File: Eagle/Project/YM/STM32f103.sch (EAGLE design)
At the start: 76 parts, among them IC1 YM3812, IC10 YM3812, IC11 YM3014B, IC12 LM358N, IC13 BA033CC0T, IC14 74ALS04N, IC15 6N136, IC2 YM3014B, IC3 LM358N, IC4 YM3812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

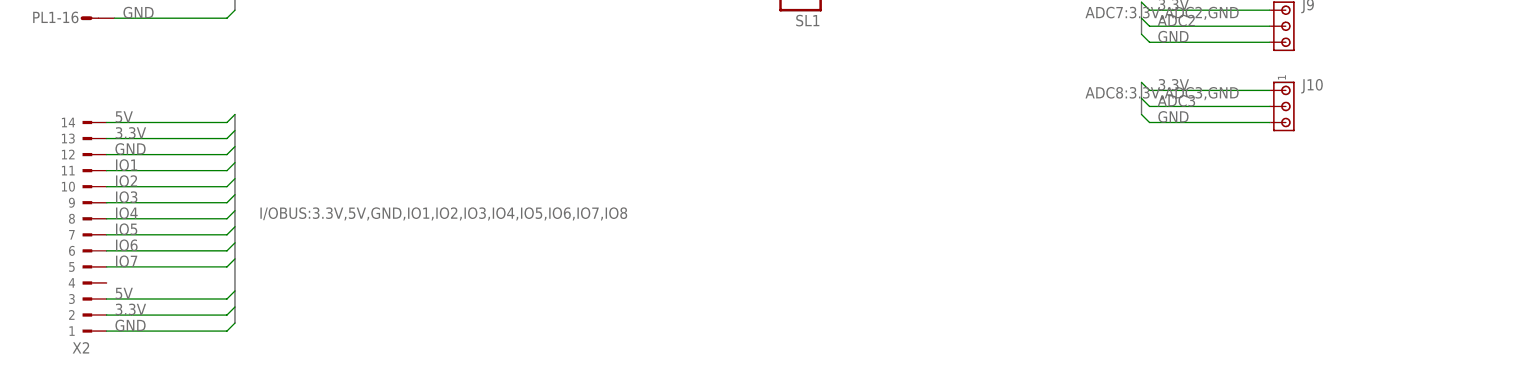
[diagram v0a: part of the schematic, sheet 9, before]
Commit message: LCD BOOTLOADER HEADER
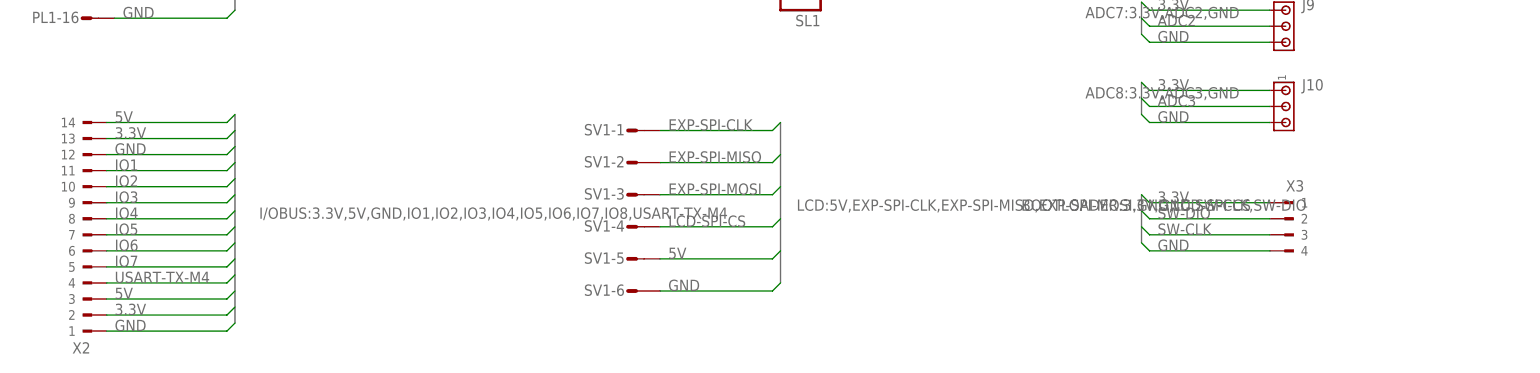
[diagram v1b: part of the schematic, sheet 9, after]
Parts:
- added SV1: (no value), con-amp-mt:S06P
- added X3: (no value), con-weidmueller-sl35:90F-4
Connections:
- new net LCD-SPI-CS: SV1-4.S, U1PORTA_L.PA2
- net 3.3V: now also X3.1
- net 5V: now also SV1-5.S
- net EXP-SPI-CLK: now also SV1-1.S
- net EXP-SPI-MISO: now also SV1-2.S
- net EXP-SPI-MOSI: now also SV1-3.S
- net GND: now also SV1-6.S, X3.4
- net IO7: no longer U1PORTA_L.PA2
- net SW-CLK: now also X3.3
- net SW-DIO: now also X3.2
- net USART-TX-M4: now also X2.4
- net YM1-CS: no longer U1PORTC_H.PC10
- net YM2-CS: now also U1PORTC_H.PC10

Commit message: Eerste versie PCB - Nog niet gerout/gerouted/geroutedt. Ter review voor plaatsing componenten.
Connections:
- removed net N$28: C39.2
- net 5V: now also C39.2
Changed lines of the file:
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@@
 <pinref part="IC14" gate="P" pin="VCC"/>
 <wire x1="175.26" y1="101.6" x2="208.28" y2="101.6" width="0.1524" layer="91"/>
+<pinref part="C39" gate="G$1" pin="2"/>
+<wire x1="208.28" y1="93.98" x2="208.28" y2="101.6" width="0.1524" layer="91"/>
+<wire x1="208.28" y1="101.6" x2="208.28" y2="109.22" width="0.1524" layer="91"/>
+<junction x="208.28" y="101.6"/>
 </segment>
 </net>
@@
 </segment>
 </net>
-<net name="N$28" class="0">
-<segment>
-<pinref part="C39" gate="G$1" pin="2"/>
-<wire x1="208.28" y1="93.98" x2="208.28" y2="109.22" width="0.1524" layer="91"/>
-</segment>
-</net>

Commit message: Opamp wire change
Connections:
- removed net N$13: C29.1, IC11.MP, IC12B.-IN
- new net N$15: C13.1, IC2.RB, IC3B.+IN
- net N$10: now also C28.1, IC11.RB, IC12B.+IN; no longer C24.1, IC8.MP, IC9B.-IN
- net N$11: now also C24.1, IC8.MP, IC9B.-IN; no longer C23.1, IC8.RB, IC9B.+IN
- net N$14: now also C29.1, IC11.MP, IC12B.-IN; no longer C28.1, IC11.RB, IC12B.+IN
- net N$4: now also C18.1, IC5.RB, IC6B.+IN; no longer C14.1, IC2.MP, IC3B.-IN
- net N$5: now also C14.1, IC2.MP, IC3B.-IN; no longer C13.1, IC2.RB, IC3B.+IN
- net N$7: now also C23.1, IC8.RB, IC9B.+IN; no longer C19.1, IC5.MP, IC6B.-IN
- net N$8: now also C19.1, IC5.MP, IC6B.-IN; no longer C18.1, IC5.RB, IC6B.+IN

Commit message: v2.0 - voldoet aan de DRC van JLPCB - PCB staat klaar voor review project groep.
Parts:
- removed X3: (no value), con-weidmueller-sl35:90F-4
- added SV2: (no value), con-lstb:MA04-1
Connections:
- net 3.3V: now also SV2.1; no longer X3.1
- net GND: now also SV2.4; no longer X3.4
- net SW-CLK: now also SV2.3; no longer X3.3
- net SW-DIO: now also SV2.2; no longer X3.2
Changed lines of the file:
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@@
 <part name="SL1" library="con-amp-quick" library_urn="urn:adsk.eagle:library:125" deviceset="M16" device="" package3d_urn="urn:adsk.eagle:package:5969/1"/>
 <part name="SV1" library="con-amp-mt" library_urn="urn:adsk.eagle:library:123" deviceset="S06P" device="" package3d_urn="urn:adsk.eagle:package:5792/1"/>
-<part name="X3" library="con-weidmueller-sl35" library_urn="urn:adsk.eagle:library:199" deviceset="90F-4" device="" package3d_urn="urn:adsk.eagle:package:11425/1"/>
+<part name="SV2" library="con-lstb" library_urn="urn:adsk.eagle:library:162" deviceset="MA04-1" device="" package3d_urn="urn:adsk.eagle:package:8337/1"/>
 </parts>
 <sheets>
@@
 <attribute name="VALUE" x="115.824" y="31.877" size="1.778" layer="96"/>
 </instance>
-<instance part="X3" gate="G$1" x="219.71" y="45.72" smashed="yes">
-<attribute name="NAME" x="219.71" y="50.038" size="1.778" layer="95"/>
-<attribute name="VALUE" x="219.71" y="37.084" size="1.778" layer="96"/>
+<instance part="SV2" gate="1" x="226.06" y="43.18" smashed="yes" rot="R180">
+<attribute name="VALUE" x="227.33" y="53.34" size="1.778" layer="96" rot="R180"/>
+<attribute name="NAME" x="227.33" y="37.338" size="1.778" layer="95" rot="R180"/>
 </instance>
 </instances>
@@
 </segment>
 <segment>
-<pinref part="X3" gate="G$1" pin="1"/>
-<wire x1="217.17" y1="48.26" x2="198.12" y2="48.26" width="0.1524" layer="91"/>
+<wire x1="218.44" y1="48.26" x2="198.12" y2="48.26" width="0.1524" layer="91"/>
 <wire x1="198.12" y1="48.26" x2="196.85" y2="49.53" width="0.1524" layer="91"/>
 <label x="199.39" y="48.26" size="1.778" layer="95"/>
+<pinref part="SV2" gate="1" pin="1"/>
 </segment>
 </net>
@@
 </segment>
 <segment>
-<pinref part="X3" gate="G$1" pin="4"/>
-<wire x1="217.17" y1="40.64" x2="198.12" y2="40.64" width="0.1524" layer="91"/>
+<wire x1="218.44" y1="40.64" x2="198.12" y2="40.64" width="0.1524" layer="91"/>
 <wire x1="198.12" y1="40.64" x2="196.85" y2="41.91" width="0.1524" layer="91"/>
 <label x="199.39" y="40.64" size="1.778" layer="95"/>
+<pinref part="SV2" gate="1" pin="4"/>
 </segment>
 </net>
@@
 <net name="SW-DIO" class="0">
 <segment>
-<pinref part="X3" gate="G$1" pin="2"/>
-<wire x1="217.17" y1="45.72" x2="198.12" y2="45.72" width="0.1524" layer="91"/>
+<wire x1="218.44" y1="45.72" x2="198.12" y2="45.72" width="0.1524" layer="91"/>
 <wire x1="198.12" y1="45.72" x2="196.85" y2="46.99" width="0.1524" layer="91"/>
 <label x="199.39" y="45.72" size="1.778" layer="95"/>
+<pinref part="SV2" gate="1" pin="2"/>
 </segment>
 </net>
 <net name="SW-CLK" class="0">
 <segment>
-<pinref part="X3" gate="G$1" pin="3"/>
-<wire x1="217.17" y1="43.18" x2="198.12" y2="43.18" width="0.1524" layer="91"/>
+<wire x1="218.44" y1="43.18" x2="198.12" y2="43.18" width="0.1524" layer="91"/>
 <wire x1="198.12" y1="43.18" x2="196.85" y2="44.45" width="0.1524" layer="91"/>
 <label x="199.39" y="43.18" size="1.778" layer="95"/>
+<pinref part="SV2" gate="1" pin="3"/>
 </segment>
 </net>

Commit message: v2.5 - IO expander update - moet nog steeds gepeerreviewd worden.
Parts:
- removed PL1: (no value), con-harting-v:16VS
- added SV3: 2514-6002UB, 2514-6002UB:2514-6002UB
- C10, C9: value (none) -> 20pF
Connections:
- removed net EXP-SPI-A0: PL1-7.S, U1PORTC_L.PC6
- removed net EXP-SPI-A1: PL1-8.S, U1PORTC_L.PC7
- removed net EXP-SPI-NSS: PL1-12.S, U1PORTB_H.PB12
- removed net EXP3-INTA: PL1-5.S, U1PORTA_H.PA11
- removed net EXP3-INTB: PL1-6.S, U1PORTA_H.PA12
- new net EXP-SPI-NSS0: SV3.11, U1PORTC_L.PC6
- new net EXP-SPI-NSS1: SV3.10, U1PORTC_L.PC7
- new net OPEN: SV3.1
- net 3.3V: now also SV3.4; no longer PL1-14.S
- net 5V: now also SV3.3; no longer PL1-15.S
- net EXP-RST: now also SV3.9; no longer PL1-13.S
- net EXP-SPI-CLK: now also SV3.14; no longer PL1-9.S
- net EXP-SPI-MISO: now also SV3.13; no longer PL1-10.S
- net EXP-SPI-MOSI: now also SV3.12; no longer PL1-11.S
- net EXP1-INTA: now also SV3.8; no longer PL1-1.S
- net EXP1-INTB: now also SV3.7; no longer PL1-2.S
- net EXP2-INTA: now also SV3.5; no longer PL1-3.S
- net EXP2-INTB: now also SV3.6; no longer PL1-4.S
- net GND: now also SV3.2; no longer PL1-16.S
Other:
- moved on the sheet: C12, C17, C22, C27, U1PORTA_H, U1PORTC_H, U1PORTC_L

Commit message: v3.0 - PCB review aangepast
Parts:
- removed X2: (no value), con-weidmueller-sl35:180G-14
- added SV4: (no value), con-lsta:FE13-1
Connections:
- removed net IO7: X2.5
- net 3.3V: now also SV4.12, SV4.2; no longer X2.13, X2.2
- net 5V: now also SV4.13, SV4.3; no longer X2.14, X2.3
- net GND: now also SV4.1, SV4.11; no longer X2.1, X2.12
- net IO1: now also SV4.10; no longer X2.11
- net IO2: now also SV4.9; no longer X2.10
- net IO3: now also SV4.8; no longer X2.9
- net IO4: now also SV4.7; no longer X2.8
- net IO5: now also SV4.6; no longer X2.7
- net IO6: now also SV4.5; no longer X2.6
- net USART-TX-M4: now also SV4.4; no longer X2.4
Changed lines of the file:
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@@
 <part name="J9" library="con-amp" library_urn="urn:adsk.eagle:library:127" deviceset="MTA03-156" device="" package3d_urn="urn:adsk.eagle:package:8081563/1"/>
 <part name="J10" library="con-amp" library_urn="urn:adsk.eagle:library:127" deviceset="MTA03-156" device="" package3d_urn="urn:adsk.eagle:package:8081563/1"/>
-<part name="X2" library="con-weidmueller-sl35" library_urn="urn:adsk.eagle:library:199" deviceset="180G-14" device="" package3d_urn="urn:adsk.eagle:package:11378/1"/>
 <part name="J2" library="SparkFun-Connectors" library_urn="urn:adsk.eagle:library:513" deviceset="DIN5" device="" package3d_urn="urn:adsk.eagle:package:38294/1"/>
 <part name="D1" library="BAT20JFILM" deviceset="BAT20JFILM" device=""/>
@@
 <part name="SV2" library="con-lstb" library_urn="urn:adsk.eagle:library:162" deviceset="MA04-1" device="" package3d_urn="urn:adsk.eagle:package:8337/1"/>
 <part name="SV3" library="2514-6002UB" deviceset="2514-6002UB" device=""/>
+<part name="SV4" library="con-lsta" library_urn="urn:adsk.eagle:library:161" deviceset="FE13-1" device="" package3d_urn="urn:adsk.eagle:package:8213/1"/>
 </parts>
 <sheets>
@@
 <attribute name="VALUE" x="215.9" y="58.42" size="1.778" layer="96" rot="R270"/>
 </instance>
-<instance part="X2" gate="G$1" x="30.48" y="43.18" smashed="yes" rot="R180">
-<attribute name="NAME" x="30.48" y="26.162" size="1.778" layer="95" rot="R180"/>
-<attribute name="VALUE" x="30.48" y="64.516" size="1.778" layer="96" rot="R180"/>
-</instance>
 <instance part="SL2" gate="G$1" x="140.97" y="142.24" smashed="yes" rot="R180">
 <attribute name="VALUE" x="146.05" y="152.4" size="1.778" layer="96" rot="R180"/>
@@
 <attribute name="VALUE" x="45.6184" y="119.761" size="2.0828" layer="96" ratio="10" rot="SR0"/>
 </instance>
+<instance part="SV4" gate="G$1" x="29.21" y="86.36" smashed="yes">
+<attribute name="VALUE" x="27.94" y="66.04" size="1.778" layer="96"/>
+<attribute name="NAME" x="27.94" y="104.902" size="1.778" layer="95"/>
+</instance>
 </instances>
 <busses>
@@
 </segment>
 </bus>
-<bus name="I/OBUS:3.3V,5V,GND,IO1,IO2,IO3,IO4,IO5,IO6,IO7,IO8,USART-TX-M4">
-<segment>
-<wire x1="53.34" y1="62.23" x2="53.34" y2="29.21" width="0.762" layer="92"/>
-<label x="57.15" y="45.72" size="1.778" layer="95"/>
-</segment>
-</bus>
 <bus name="YM-DIG-OUTPUT:5V,GND,USART-RX-M4,USART-TX-M4,YM1-CLK-O,YM1-CS,YM1-OUTPUT,YM1-SYNC,YM2-CLK-O,YM2-OUTPUT,YM2-SYNC,YM3-CLK-O,YM3-OUTPUT,YM3-SYNC,YM4-CLK-O,YM4-OUTPUT,YM4-SYNC">
 <segment>
@@
 <net name="5V" class="0">
 <segment>
-<wire x1="33.02" y1="60.96" x2="52.07" y2="60.96" width="0.1524" layer="91"/>
-<wire x1="52.07" y1="60.96" x2="53.34" y2="62.23" width="0.1524" layer="91"/>
-<label x="34.29" y="60.96" size="1.778" layer="95"/>
-<pinref part="X2" gate="G$1" pin="14"/>
-</segment>
-<segment>
-<pinref part="X2" gate="G$1" pin="3"/>
-<wire x1="33.02" y1="33.02" x2="52.07" y2="33.02" width="0.1524" layer="91"/>
-<wire x1="52.07" y1="33.02" x2="53.34" y2="34.29" width="0.1524" layer="91"/>
-<label x="34.29" y="33.02" size="1.778" layer="95"/>
-</segment>
-<segment>
 <pinref part="SL1" gate="G$1" pin="15"/>
 <wire x1="135.89" y1="83.82" x2="116.84" y2="83.82" width="0.1524" layer="91"/>
@@
 <wire x1="31.75" y1="142.24" x2="13.97" y2="142.24" width="0.1524" layer="91"/>
 </segment>
+<segment>
+<pinref part="SV4" gate="G$1" pin="13"/>
+<wire x1="36.83" y1="101.6" x2="54.61" y2="101.6" width="0.1524" layer="91"/>
+<label x="38.1" y="101.6" size="1.778" layer="95"/>
+</segment>
+<segment>
+<pinref part="SV4" gate="G$1" pin="3"/>
+<wire x1="36.83" y1="76.2" x2="54.61" y2="76.2" width="0.1524" layer="91"/>
+<label x="38.1" y="76.2" size="1.778" layer="95"/>
+</segment>
 </net>
 <net name="3.3V" class="0">
@@
 </segment>
 <segment>
-<wire x1="33.02" y1="58.42" x2="52.07" y2="58.42" width="0.1524" layer="91"/>
-<wire x1="52.07" y1="58.42" x2="53.34" y2="59.69" width="0.1524" layer="91"/>
-<label x="34.29" y="58.42" size="1.778" layer="95"/>
-<pinref part="X2" gate="G$1" pin="13"/>
-</segment>
-<segment>
-<pinref part="X2" gate="G$1" pin="2"/>
-<wire x1="33.02" y1="30.48" x2="52.07" y2="30.48" width="0.1524" layer="91"/>
-<wire x1="52.07" y1="30.48" x2="53.34" y2="31.75" width="0.1524" layer="91"/>
-<label x="34.29" y="30.48" size="1.778" layer="95"/>
-</segment>
-<segment>
 <wire x1="218.44" y1="48.26" x2="198.12" y2="48.26" width="0.1524" layer="91"/>
 <wire x1="198.12" y1="48.26" x2="196.85" y2="49.53" width="0.1524" layer="91"/>
@@
 <wire x1="67.31" y1="142.24" x2="85.09" y2="142.24" width="0.1524" layer="91"/>
 </segment>
+<segment>
+<pinref part="SV4" gate="G$1" pin="12"/>
+<wire x1="36.83" y1="99.06" x2="54.61" y2="99.06" width="0.1524" layer="91"/>
+<label x="38.1" y="99.06" size="1.778" layer="95"/>
+</segment>
+<segment>
+<pinref part="SV4" gate="G$1" pin="2"/>
+<wire x1="36.83" y1="73.66" x2="54.61" y2="73.66" width="0.1524" layer="91"/>
+<label x="38.1" y="73.66" size="1.778" layer="95"/>
+</segment>
 </net>
 <net name="GND" class="0">
@@
 </segment>
 <segment>
-<wire x1="33.02" y1="55.88" x2="52.07" y2="55.88" width="0.1524" layer="91"/>
-<wire x1="52.07" y1="55.88" x2="53.34" y2="57.15" width="0.1524" layer="91"/>
-<label x="34.29" y="55.88" size="1.778" layer="95"/>
-<pinref part="X2" gate="G$1" pin="12"/>
-</segment>
-<segment>
-<pinref part="X2" gate="G$1" pin="1"/>
-<wire x1="33.02" y1="27.94" x2="52.07" y2="27.94" width="0.1524" layer="91"/>
-<wire x1="52.07" y1="27.94" x2="53.34" y2="29.21" width="0.1524" layer="91"/>
-<label x="34.29" y="27.94" size="1.778" layer="95"/>
-</segment>
-<segment>
 <wire x1="135.89" y1="134.62" x2="116.84" y2="134.62" width="0.1524" layer="91"/>
 <label x="119.38" y="134.62" size="1.778" layer="95"/>
@@
 <wire x1="67.31" y1="144.78" x2="85.09" y2="144.78" width="0.1524" layer="91"/>
 </segment>
+<segment>
+<pinref part="SV4" gate="G$1" pin="11"/>
+<wire x1="36.83" y1="96.52" x2="54.61" y2="96.52" width="0.1524" layer="91"/>
+<label x="38.1" y="96.52" size="1.778" layer="95"/>
+</segment>
+<segment>
+<pinref part="SV4" gate="G$1" pin="1"/>
+<wire x1="36.83" y1="71.12" x2="54.61" y2="71.12" width="0.1524" layer="91"/>
+<label x="38.1" y="71.12" size="1.778" layer="95"/>
+</segment>
 </net>
 <net name="ADC-VOL-TOT" class="0">
@@
 <net name="IO1" class="0">
 <segment>
-<wire x1="33.02" y1="53.34" x2="52.07" y2="53.34" width="0.1524" layer="91"/>
-<wire x1="52.07" y1="53.34" x2="53.34" y2="54.61" width="0.1524" layer="91"/>
-<label x="34.29" y="53.34" size="1.778" layer="95"/>
-<pinref part="X2" gate="G$1" pin="11"/>
+<pinref part="SV4" gate="G$1" pin="10"/>
+<wire x1="36.83" y1="93.98" x2="54.61" y2="93.98" width="0.1524" layer="91"/>
+<label x="38.1" y="93.98" size="1.778" layer="95"/>
 </segment>
 </net>
 <net name="IO2" class="0">
 <segment>
-<wire x1="33.02" y1="50.8" x2="52.07" y2="50.8" width="0.1524" layer="91"/>
-<wire x1="52.07" y1="50.8" x2="53.34" y2="52.07" width="0.1524" layer="91"/>
-<label x="34.29" y="50.8" size="1.778" layer="95"/>
-<pinref part="X2" gate="G$1" pin="10"/>
+<pinref part="SV4" gate="G$1" pin="9"/>
+<wire x1="36.83" y1="91.44" x2="54.61" y2="91.44" width="0.1524" layer="91"/>
+<label x="38.1" y="91.44" size="1.778" layer="95"/>
 </segment>
 </net>
 <net name="IO3" class="0">
 <segment>
-<wire x1="33.02" y1="48.26" x2="52.07" y2="48.26" width="0.1524" layer="91"/>
-<wire x1="52.07" y1="48.26" x2="53.34" y2="49.53" width="0.1524" layer="91"/>
-<label x="34.29" y="48.26" size="1.778" layer="95"/>
-<pinref part="X2" gate="G$1" pin="9"/>
+<pinref part="SV4" gate="G$1" pin="8"/>
+<wire x1="36.83" y1="88.9" x2="54.61" y2="88.9" width="0.1524" layer="91"/>
+<label x="38.1" y="88.9" size="1.778" layer="95"/>
 </segment>
 </net>
 <net name="IO4" class="0">
 <segment>
-<wire x1="33.02" y1="45.72" x2="52.07" y2="45.72" width="0.1524" layer="91"/>
-<wire x1="52.07" y1="45.72" x2="53.34" y2="46.99" width="0.1524" layer="91"/>
-<label x="34.29" y="45.72" size="1.778" layer="95"/>
-<pinref part="X2" gate="G$1" pin="8"/>
+<pinref part="SV4" gate="G$1" pin="7"/>
+<wire x1="36.83" y1="86.36" x2="54.61" y2="86.36" width="0.1524" layer="91"/>
+<label x="38.1" y="86.36" size="1.778" layer="95"/>
 </segment>
 </net>
 <net name="IO5" class="0">
 <segment>
-<wire x1="33.02" y1="43.18" x2="52.07" y2="43.18" width="0.1524" layer="91"/>
-<wire x1="52.07" y1="43.18" x2="53.34" y2="44.45" width="0.1524" layer="91"/>
-<pinref part="X2" gate="G$1" pin="7"/>
-<label x="34.29" y="43.18" size="1.778" layer="95"/>
+<pinref part="SV4" gate="G$1" pin="6"/>
+<wire x1="36.83" y1="83.82" x2="54.61" y2="83.82" width="0.1524" layer="91"/>
+<label x="38.1" y="83.82" size="1.778" layer="95"/>
 </segment>
 </net>
 <net name="IO6" class="0">
 <segment>
-<wire x1="33.02" y1="40.64" x2="52.07" y2="40.64" width="0.1524" layer="91"/>
-<wire x1="52.07" y1="40.64" x2="53.34" y2="41.91" width="0.1524" layer="91"/>
-<pinref part="X2" gate="G$1" pin="6"/>
-<label x="34.29" y="40.64" size="1.778" layer="95"/>
-</segment>
-</net>
-<net name="IO7" class="0">
-<segment>
-<wire x1="33.02" y1="38.1" x2="52.07" y2="38.1" width="0.1524" layer="91"/>
-<wire x1="52.07" y1="38.1" x2="53.34" y2="39.37" width="0.1524" layer="91"/>
-<pinref part="X2" gate="G$1" pin="5"/>
-<label x="34.29" y="38.1" size="1.778" layer="95"/>
+<pinref part="SV4" gate="G$1" pin="5"/>
+<wire x1="36.83" y1="81.28" x2="54.61" y2="81.28" width="0.1524" layer="91"/>
+<label x="38.1" y="81.28" size="1.778" layer="95"/>
 </segment>
 </net>
@@
 </segment>
 <segment>
-<pinref part="X2" gate="G$1" pin="4"/>
-<wire x1="33.02" y1="35.56" x2="52.07" y2="35.56" width="0.1524" layer="91"/>
-<wire x1="52.07" y1="35.56" x2="53.34" y2="36.83" width="0.1524" layer="91"/>
-<label x="34.29" y="35.56" size="1.778" layer="95"/>
+<pinref part="SV4" gate="G$1" pin="4"/>
+<wire x1="36.83" y1="78.74" x2="54.61" y2="78.74" width="0.1524" layer="91"/>
+<label x="38.1" y="78.74" size="1.778" layer="95"/>
 </segment>
 </net>
